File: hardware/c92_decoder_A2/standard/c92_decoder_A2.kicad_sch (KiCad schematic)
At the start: 13 parts, among them J10 F2_OUT, J11 F3_OUT, J12 F4_OUT, J13 GND, J14 CAP, J2 TRACK_1, J3 TRACK_2, J4 F0F_OUT, J5 F0R_OUT, J6 MOTOR_L, J7 MOTOR_R, J8 VDD, J9 F1_OUT

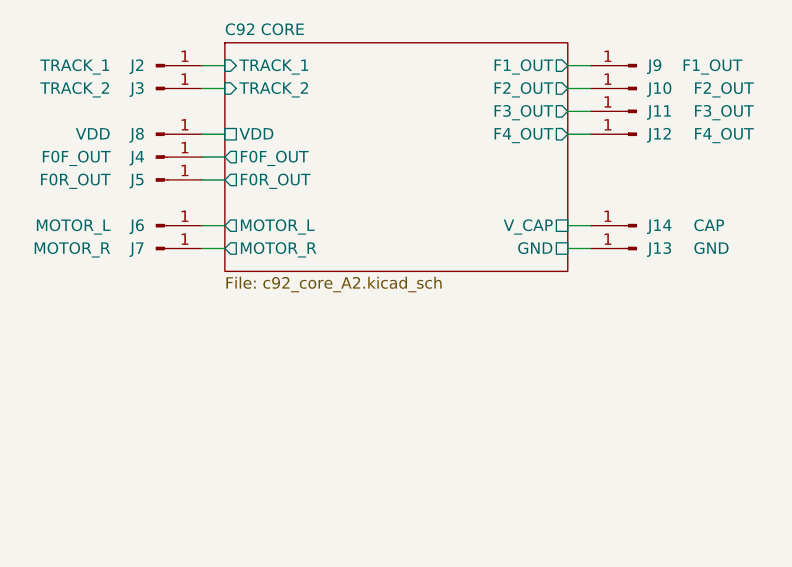
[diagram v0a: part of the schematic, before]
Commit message: new KiCAD structure for multiple variants
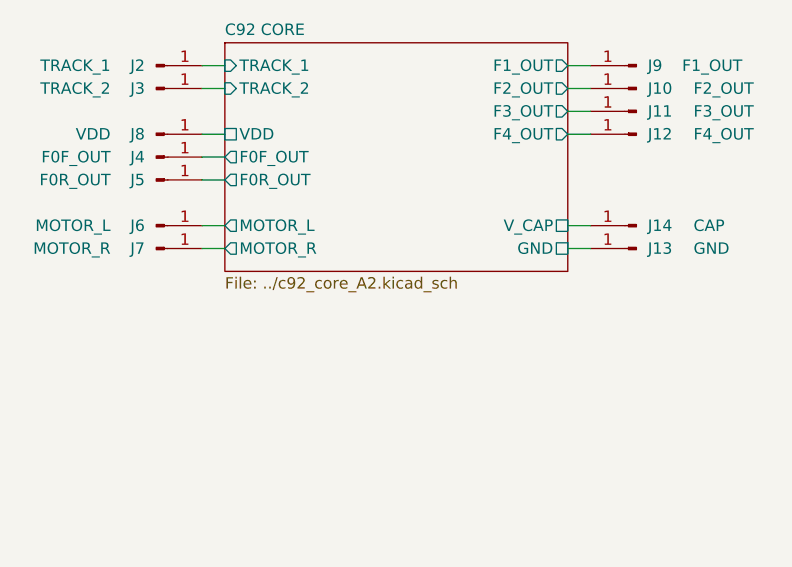
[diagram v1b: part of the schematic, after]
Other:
- sheet C92 CORE: file c92_core_A2.kicad_sch -> ../c92_core_A2.kicad_sch
- title: c92 decoder -> c92 decoder - standard
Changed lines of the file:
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@@
 	(paper "A3")
 	(title_block
-		(title "c92 decoder")
+		(title "c92 decoder - standard")
 		(date "2026-10-05")
 		(rev "REV-A2")
@@
 			)
 		)
-		(property "Sheetfile" "c92_core_A2.kicad_sch"
+		(property "Sheetfile" "../c92_core_A2.kicad_sch"
 			(at 190.5 152.9846 0)
 			(show_name no)
